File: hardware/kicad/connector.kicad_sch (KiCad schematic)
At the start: 1 part, among them J501 Conn_02x20_Counter_Clockwise

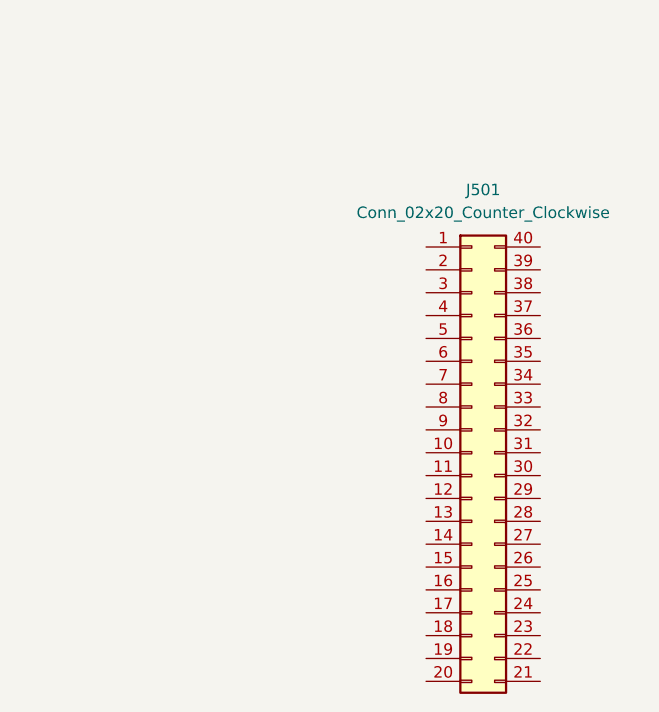
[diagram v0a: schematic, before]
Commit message: layout: finish dq0 & dq1 routing
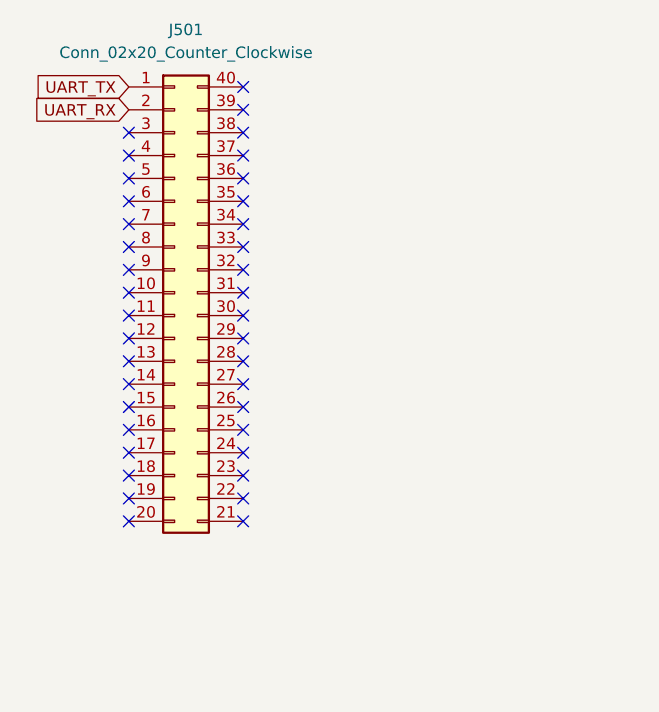
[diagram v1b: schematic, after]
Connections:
- net UART_TX: now reaches J501.1 (Pin_1)
- net UART_RX: now reaches J501.2 (Pin_2)
- no-connect marks 0 -> 38
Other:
- moved on the sheet: J501
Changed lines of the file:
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@@
 	(generator_version "10.0")
 	(paper "A4")
+	(no_connect
+		(at 29.21 49.53)
+	)
+	(no_connect
+		(at 29.21 64.77)
+	)
+	(no_connect
+		(at 29.21 46.99)
+	)
+	(no_connect
+		(at 41.91 57.15)
+	)
+	(no_connect
+		(at 41.91 72.39)
+	)
+	(no_connect
+		(at 41.91 36.83)
+	)
+	(no_connect
+		(at 41.91 64.77)
+	)
+	(no_connect
+		(at 29.21 54.61)
+	)
+	(no_connect
+		(at 29.21 67.31)
+	)
+	(no_connect
+		(at 41.91 74.93)
+	)
+	(no_connect
+		(at 29.21 52.07)
+	)
+	(no_connect
+		(at 41.91 59.69)
+	)
+	(no_connect
+		(at 41.91 52.07)
+	)
+	(no_connect
+		(at 29.21 77.47)
+	)
+	(no_connect
+		(at 29.21 44.45)
+	)
+	(no_connect
+		(at 41.91 29.21)
+	)
+	(no_connect
+		(at 29.21 39.37)
+	)
+	(no_connect
+		(at 41.91 49.53)
+	)
+	(no_connect
+		(at 29.21 57.15)
+	)
+	(no_connect
+		(at 41.91 67.31)
+	)
+	(no_connect
+		(at 41.91 77.47)
+	)
+	(no_connect
+		(at 29.21 74.93)
+	)
+	(no_connect
+		(at 29.21 36.83)
+	)
+	(no_connect
+		(at 41.91 54.61)
+	)
+	(no_connect
+		(at 41.91 46.99)
+	)
+	(no_connect
+		(at 41.91 69.85)
+	)
+	(no_connect
+		(at 41.91 41.91)
+	)
+	(no_connect
+		(at 41.91 39.37)
+	)
+	(no_connect
+		(at 29.21 41.91)
+	)
+	(no_connect
+		(at 29.21 72.39)
+	)
+	(no_connect
+		(at 29.21 62.23)
+	)
+	(no_connect
+		(at 41.91 62.23)
+	)
+	(no_connect
+		(at 29.21 34.29)
+	)
+	(no_connect
+		(at 29.21 59.69)
+	)
+	(no_connect
+		(at 41.91 31.75)
+	)
+	(no_connect
+		(at 41.91 44.45)
+	)
+	(no_connect
+		(at 41.91 34.29)
+	)
+	(no_connect
+		(at 29.21 69.85)
+	)
+	(global_label "UART_RX"
+		(shape input)
+		(at 29.21 31.75 180)
+		(fields_autoplaced yes)
+		(effects
+			(font
+				(size 1.27 1.27)
+			)
+			(justify right)
+		)
+		(property "Intersheetrefs" "${INTERSHEET_REFS}"
+			(at 18.121 31.75 0)
+			(hide yes)
+			(show_name no)
+			(do_not_autoplace no)
+			(effects
+				(font
+					(size 1.27 1.27)
+				)
+				(justify right)
+			)
+		)
+	)
+	(global_label "UART_TX"
+		(shape input)
+		(at 29.21 29.21 180)
+		(fields_autoplaced yes)
+		(effects
+			(font
+				(size 1.27 1.27)
+			)
+			(justify right)
+		)
+		(property "Intersheetrefs" "${INTERSHEET_REFS}"
+			(at 18.4234 29.21 0)
+			(hide yes)
+			(show_name no)
+			(do_not_autoplace no)
+			(effects
+				(font
+					(size 1.27 1.27)
+				)
+				(justify right)
+			)
+		)
+	)
 	(symbol
 		(lib_id "Connector_Generic:Conn_02x20_Counter_Clockwise")
-		(at 67.31 69.85 0)
+		(at 34.29 52.07 0)
 		(unit 1)
 		(body_style 1)
@@
 		(fields_autoplaced yes)
 		(property "Reference" "J501"
-			(at 68.58 40.64 0)
+			(at 35.56 22.86 0)
 			(show_name no)
 			(do_not_autoplace no)
@@
 		)
 		(property "Value" "Conn_02x20_Counter_Clockwise"
-			(at 68.58 43.18 0)
+			(at 35.56 25.4 0)
 			(show_name no)
 			(do_not_autoplace no)
@@
 		)
 		(property "Footprint" "Connector_PinHeader_2.54mm:PinHeader_2x20_P2.54mm_Vertical"
-			(at 67.31 69.85 0)
+			(at 34.29 52.07 0)
 			(hide yes)
 			(show_name no)
@@
 		)
 		(property "Datasheet" ""
-			(at 67.31 69.85 0)
+			(at 34.29 52.07 0)
 			(hide yes)
 			(show_name no)
@@
 		)
 		(property "Description" "Generic connector, double row, 02x20, counter clockwise pin numbering scheme (similar to DIP package numbering), script generated (kicad-library-utils/schlib/autogen/connector/)"
-			(at 67.31 69.85 0)
-			(hide yes)
-			(show_name no)
+			(at 34.29 52.07 0)
+			(hide yes)
+			(show_name no)
